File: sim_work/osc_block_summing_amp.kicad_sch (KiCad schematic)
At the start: 4 parts, among them U1 LM4562

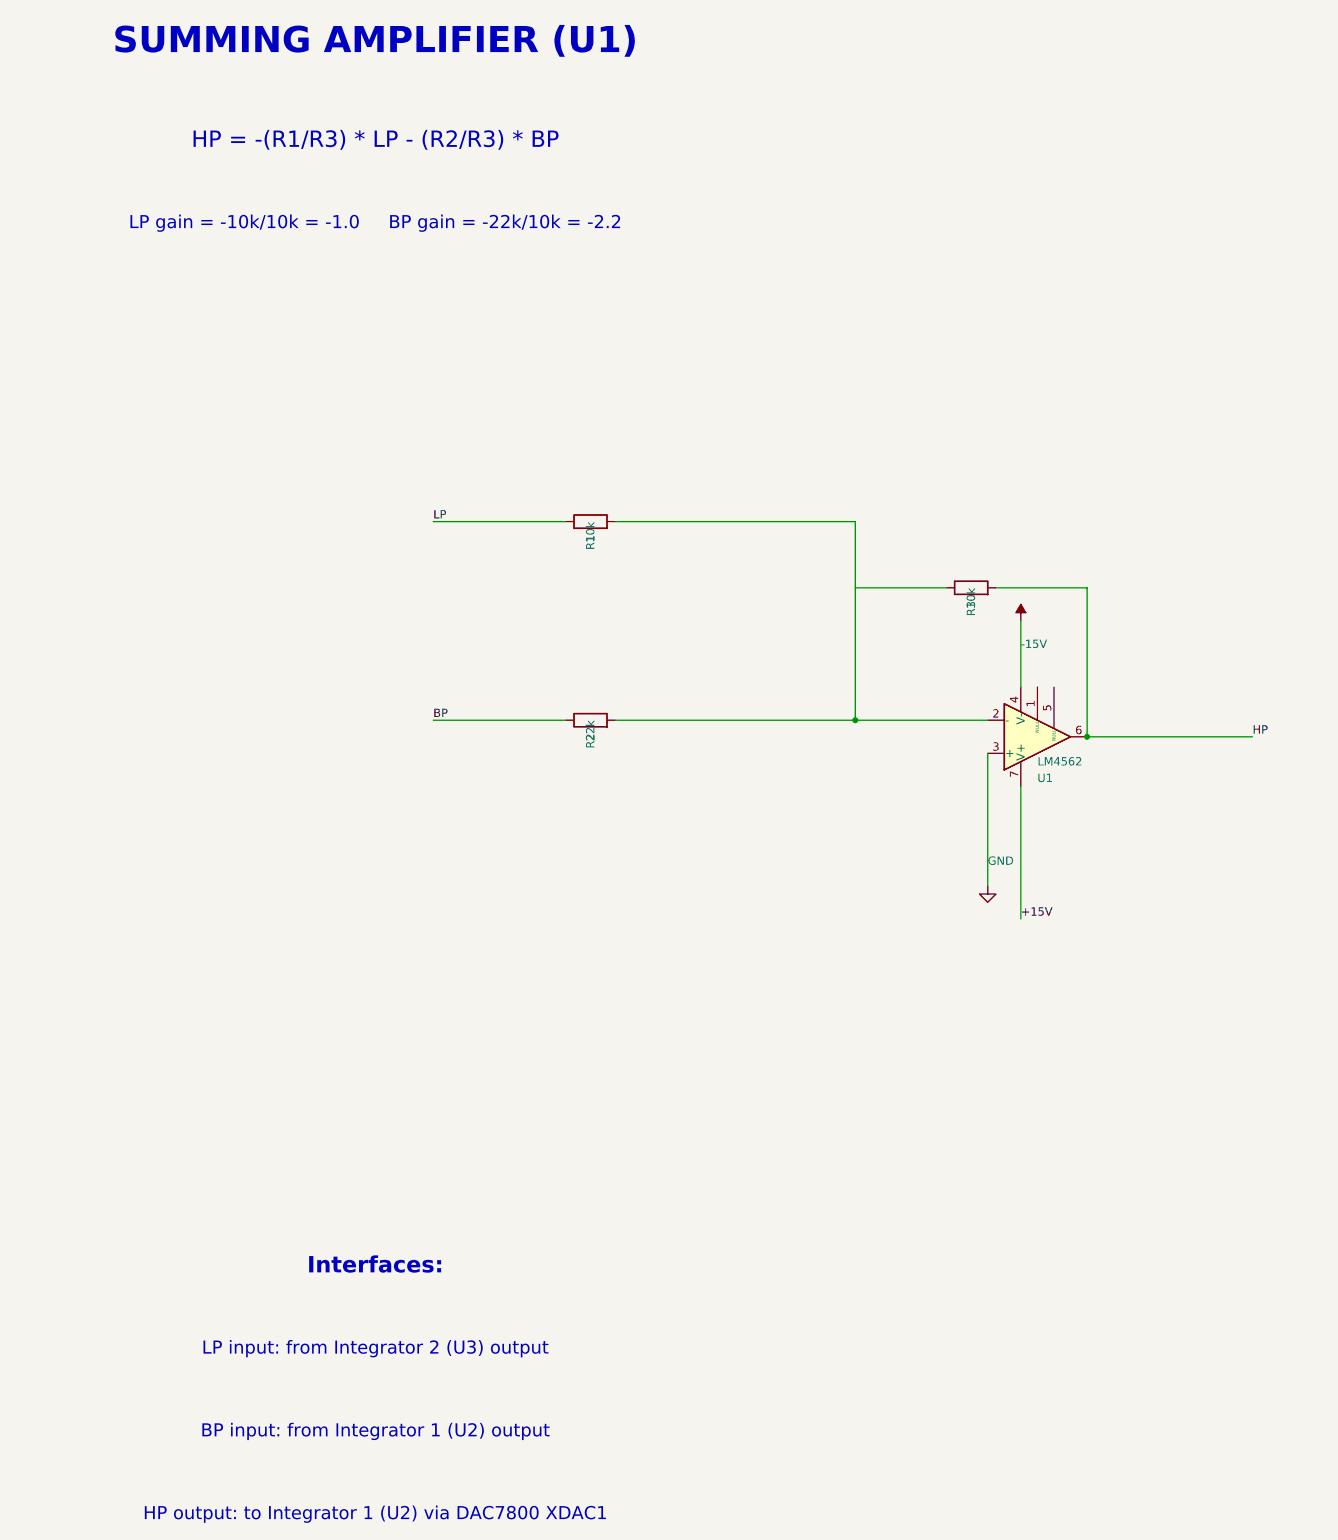
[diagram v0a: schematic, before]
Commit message: Fix schematic connections, add docs and repo portability
- Input filters: R rotation=90 (horizontal), ESD diode rotations fixed,
  junction dots at cathode-signal connection, wires to GND symbols
- Relay ladder: flyback diode rotation 270->90 (K top, A bottom)
- Electrometer/Mux TIA: 4 junction dots each at T-junctions
- AD636 RMS detector: proper IC box with pin labels replaces text-only
- Oscillator blocks: D_Zener symbol, L-shaped cathode routing
- TIA blocks: title/function annotations on all 5 blocks
- New: requirements.txt, docs/oscillator_guide.md
- D_Zener.kicad_sym added to bundled symbols/
- .gitignore updated for docs/ and requirements.txt
- README updated with pip install -r requirements.txt
- PROJECT.md session 9 changelog
- SimGUI builds clean (0 errors)

Co-Authored-By: Claude Opus 4.6 <noreply@anthropic.com>
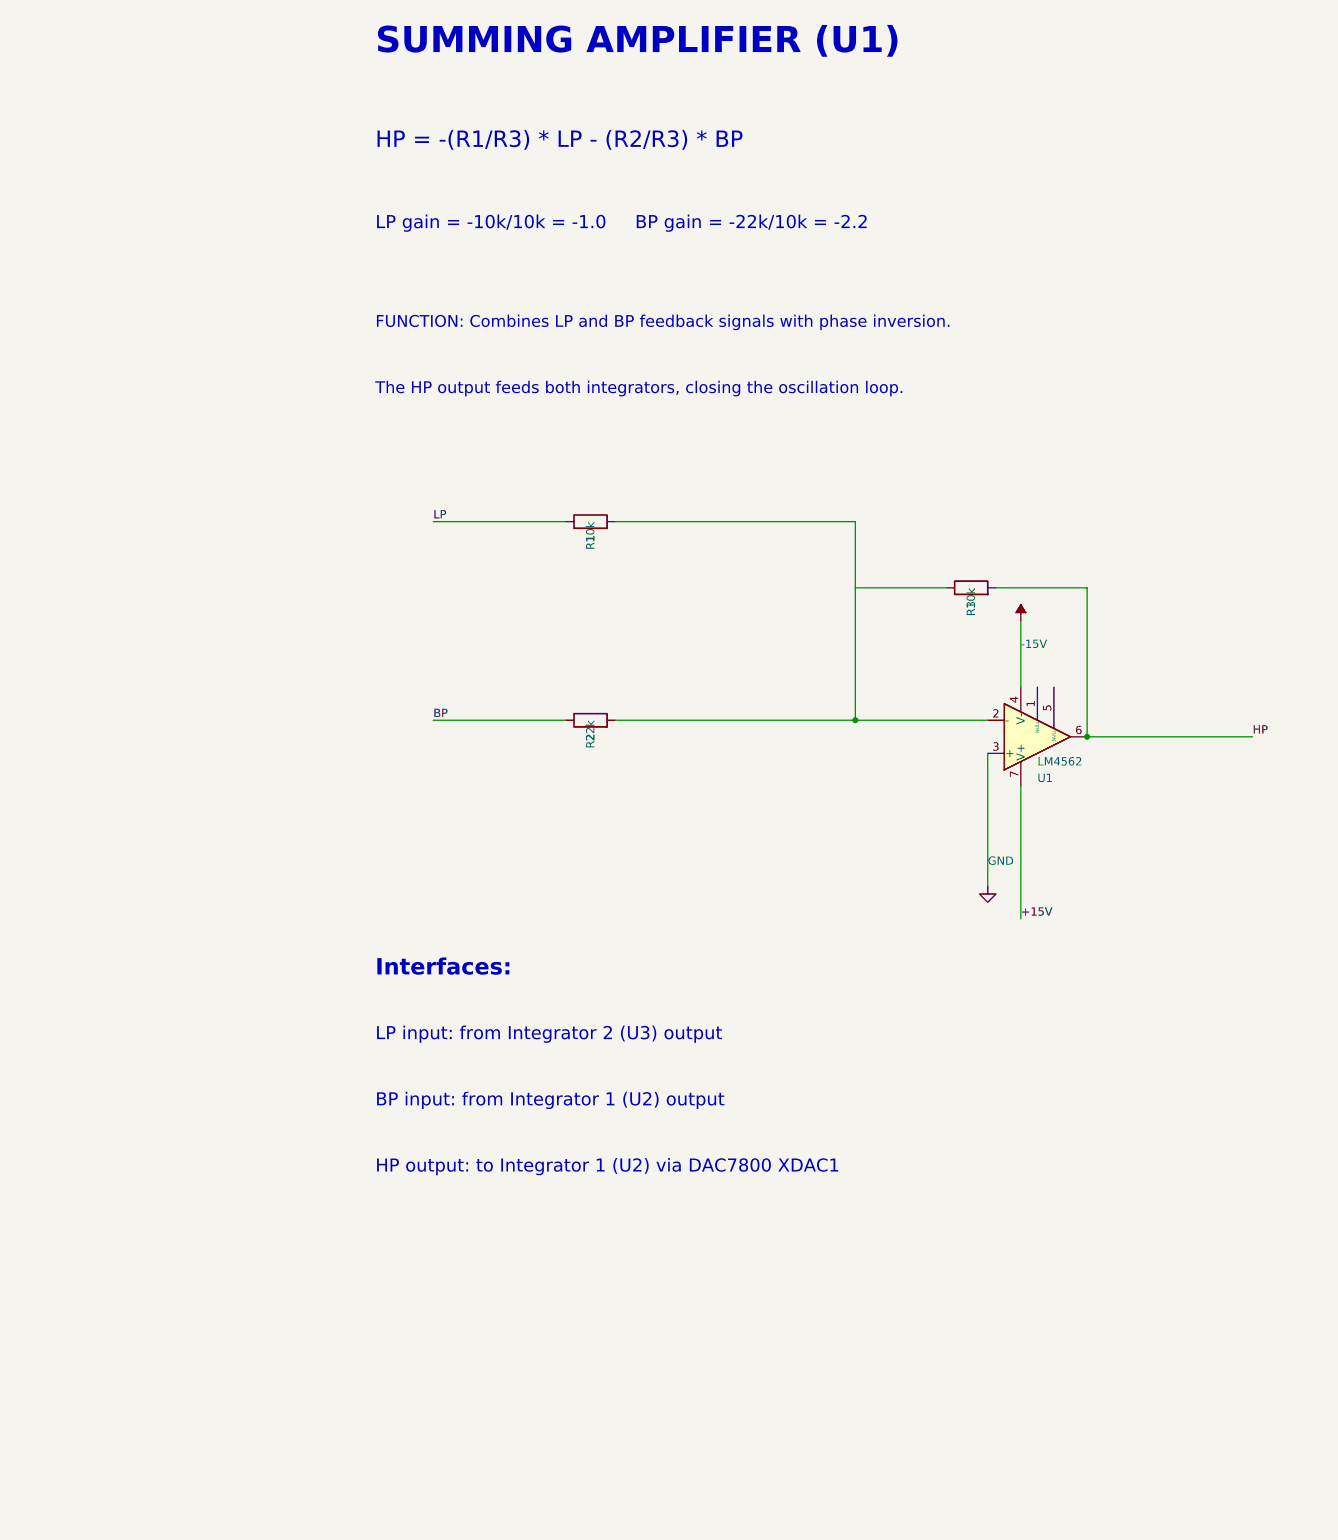
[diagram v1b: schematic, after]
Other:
- note added: "FUNCTION: Combines LP and BP feedback signals with phase inversion."
- note added: "The HP output feeds both integrators, closing the oscillation loop."
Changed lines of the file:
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@@
 		(instances
 			(project "Oscillator - Summing Amplifier"
-				(path "/2c799509-0e7d-405b-bbcf-876a6c7cc8ef"
+				(path "/fb9dc419-e6c7-4f84-8a32-7dc9712e332e"
 					(reference "U1")
 					(unit 1)
@@
 		(instances
 			(project "Oscillator - Summing Amplifier"
-				(path "/2c799509-0e7d-405b-bbcf-876a6c7cc8ef"
+				(path "/fb9dc419-e6c7-4f84-8a32-7dc9712e332e"
 					(reference "R1")
 					(unit 1)
@@
 		(instances
 			(project "Oscillator - Summing Amplifier"
-				(path "/2c799509-0e7d-405b-bbcf-876a6c7cc8ef"
+				(path "/fb9dc419-e6c7-4f84-8a32-7dc9712e332e"
 					(reference "R2")
 					(unit 1)
@@
 		(instances
 			(project "Oscillator - Summing Amplifier"
-				(path "/2c799509-0e7d-405b-bbcf-876a6c7cc8ef"
+				(path "/fb9dc419-e6c7-4f84-8a32-7dc9712e332e"
 					(reference "R3")
 					(unit 1)
@@
 		(instances
 			(project "Oscillator - Summing Amplifier"
-				(path "/2c799509-0e7d-405b-bbcf-876a6c7cc8ef"
+				(path "/fb9dc419-e6c7-4f84-8a32-7dc9712e332e"
 					(reference "#PWR001")
 					(unit 1)
@@
 		(instances
 			(project "Oscillator - Summing Amplifier"
-				(path "/2c799509-0e7d-405b-bbcf-876a6c7cc8ef"
+				(path "/fb9dc419-e6c7-4f84-8a32-7dc9712e332e"
 					(reference "#PWR002")
 					(unit 1)
@@
 				(bold yes)
 			)
+			(justify left)
 		)
 	)
@@
 				(size 2.5 2.5)
 			)
+			(justify left)
 		)
 	)
@@
 				(size 2 2)
 			)
+			(justify left)
+		)
+	)
+	(text "FUNCTION: Combines LP and BP feedback signals with phase inversion."
+		(exclude_from_sim no)
+		(at 20.32 58.42 0.0000)
+		(effects
+			(font
+				(size 1.8 1.8)
+			)
+			(justify left)
+		)
+	)
+	(text "The HP output feeds both integrators, closing the oscillation loop."
+		(exclude_from_sim no)
+		(at 20.32 68.58 0.0000)
+		(effects
+			(font
+				(size 1.8 1.8)
+			)
+			(justify left)
 		)
 	)
 	(text "Interfaces:"
 		(exclude_from_sim no)
-		(at 20.32 203.2 0.0000)
+		(at 20.32 157.48 0.0000)
 		(effects
 			(font
@@
 				(bold yes)
 			)
+			(justify left)
 		)
 	)
 	(text "LP input: from Integrator 2 (U3) output"
 		(exclude_from_sim no)
-		(at 20.32 215.9 0.0000)
+		(at 20.32 167.64 0.0000)
 		(effects
 			(font
 				(size 2 2)
 			)
+			(justify left)
 		)
 	)
 	(text "BP input: from Integrator 1 (U2) output"
 		(exclude_from_sim no)
-		(at 20.32 228.6 0.0000)
+		(at 20.32 177.8 0.0000)
 		(effects
 			(font
 				(size 2 2)
 			)
+			(justify left)
 		)
 	)
 	(text "HP output: to Integrator 1 (U2) via DAC7800 XDAC1"
 		(exclude_from_sim no)
-		(at 20.32 241.3 0.0000)
+		(at 20.32 187.96 0.0000)
 		(effects
 			(font
 				(size 2 2)
 			)
-		)
-	)
+			(justify left)
+		)
+	)

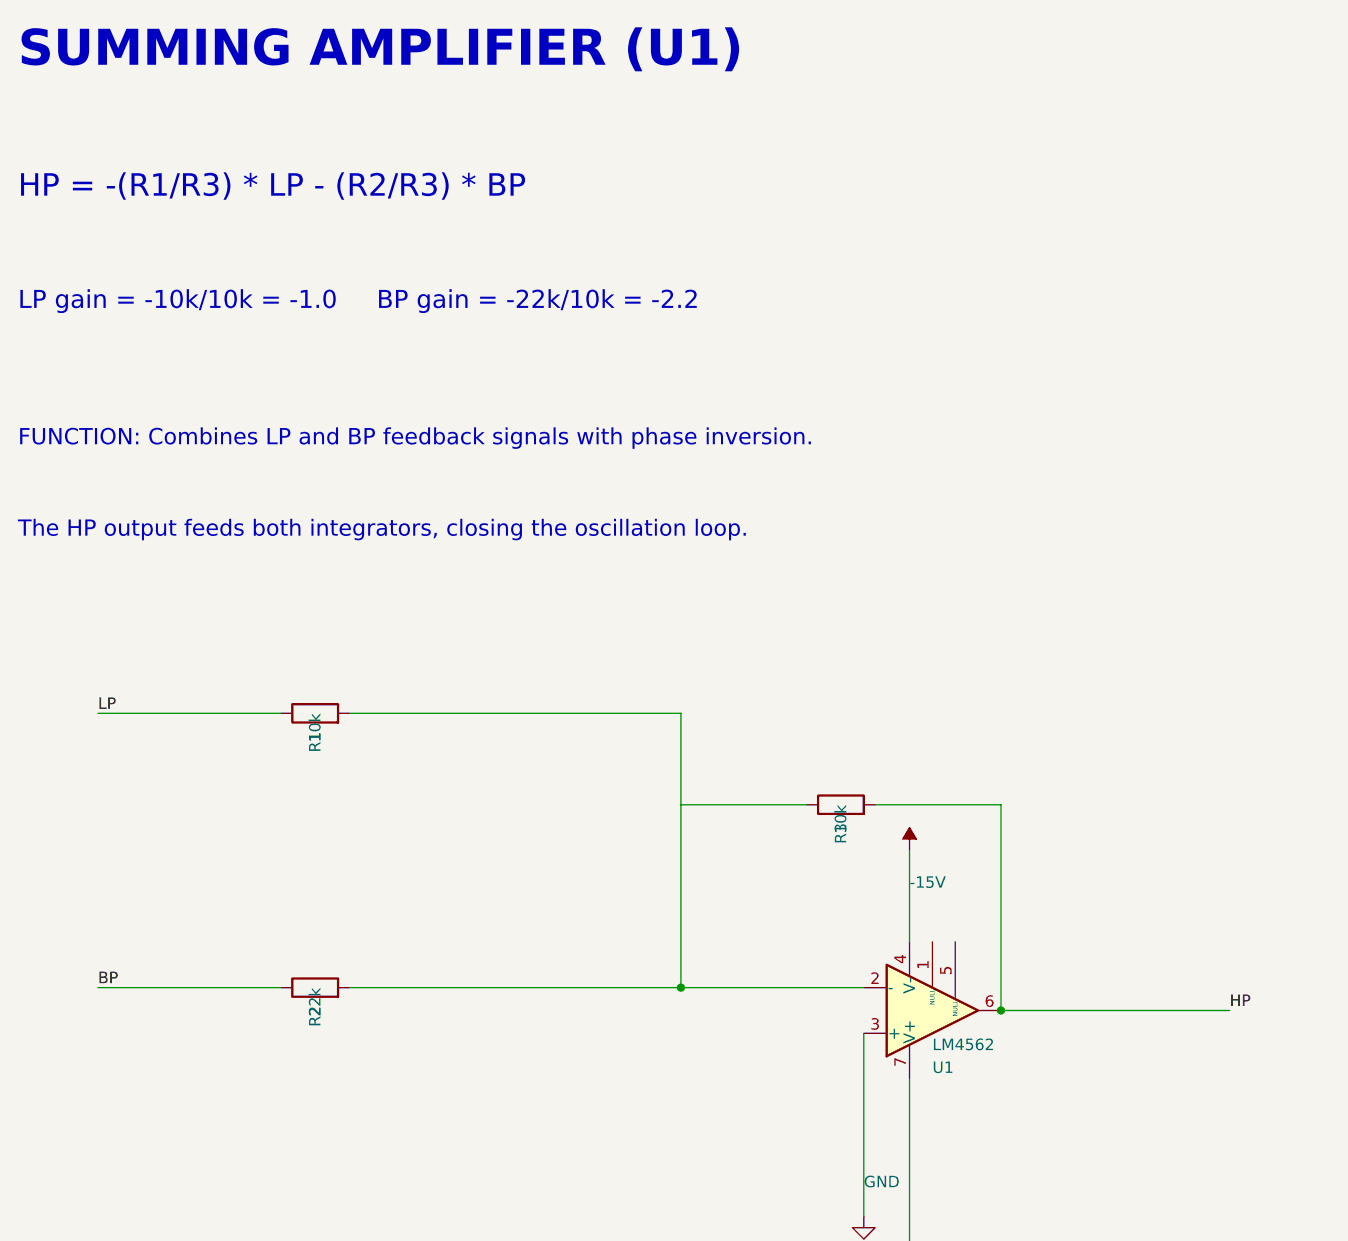
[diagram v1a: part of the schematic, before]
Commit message: Add comparison mode, fix SimGUI subprocess popups, DAC7800 IC boxes
- SimGUI: fix Python path detection (FindPython searches Python312/313/311)
- SimGUI: suppress console popup windows (CREATE_NO_WINDOW for subprocess)
- SimGUI: add Comparison project (MDAC vs Analog oscillator side-by-side)
- SimGUI: fix async wrapping (direct await instead of Task.Run)
- Pipeline: draw DAC7800 as proper IC box with pin labels (VREF/IOUT/VCTRL)
- Pipeline: fix electrometer_362 layout (spacing, junction dots at T-junctions)
- Pipeline: fix summing amp gain annotations (BP=-0.455, not -2.2)
- Pipeline: add analog_osc command for friend's SVF oscillator simulation
- Docs: comparison_guide.md, updated README and PROJECT tracker

Co-Authored-By: Claude Opus 4.6 <noreply@anthropic.com>
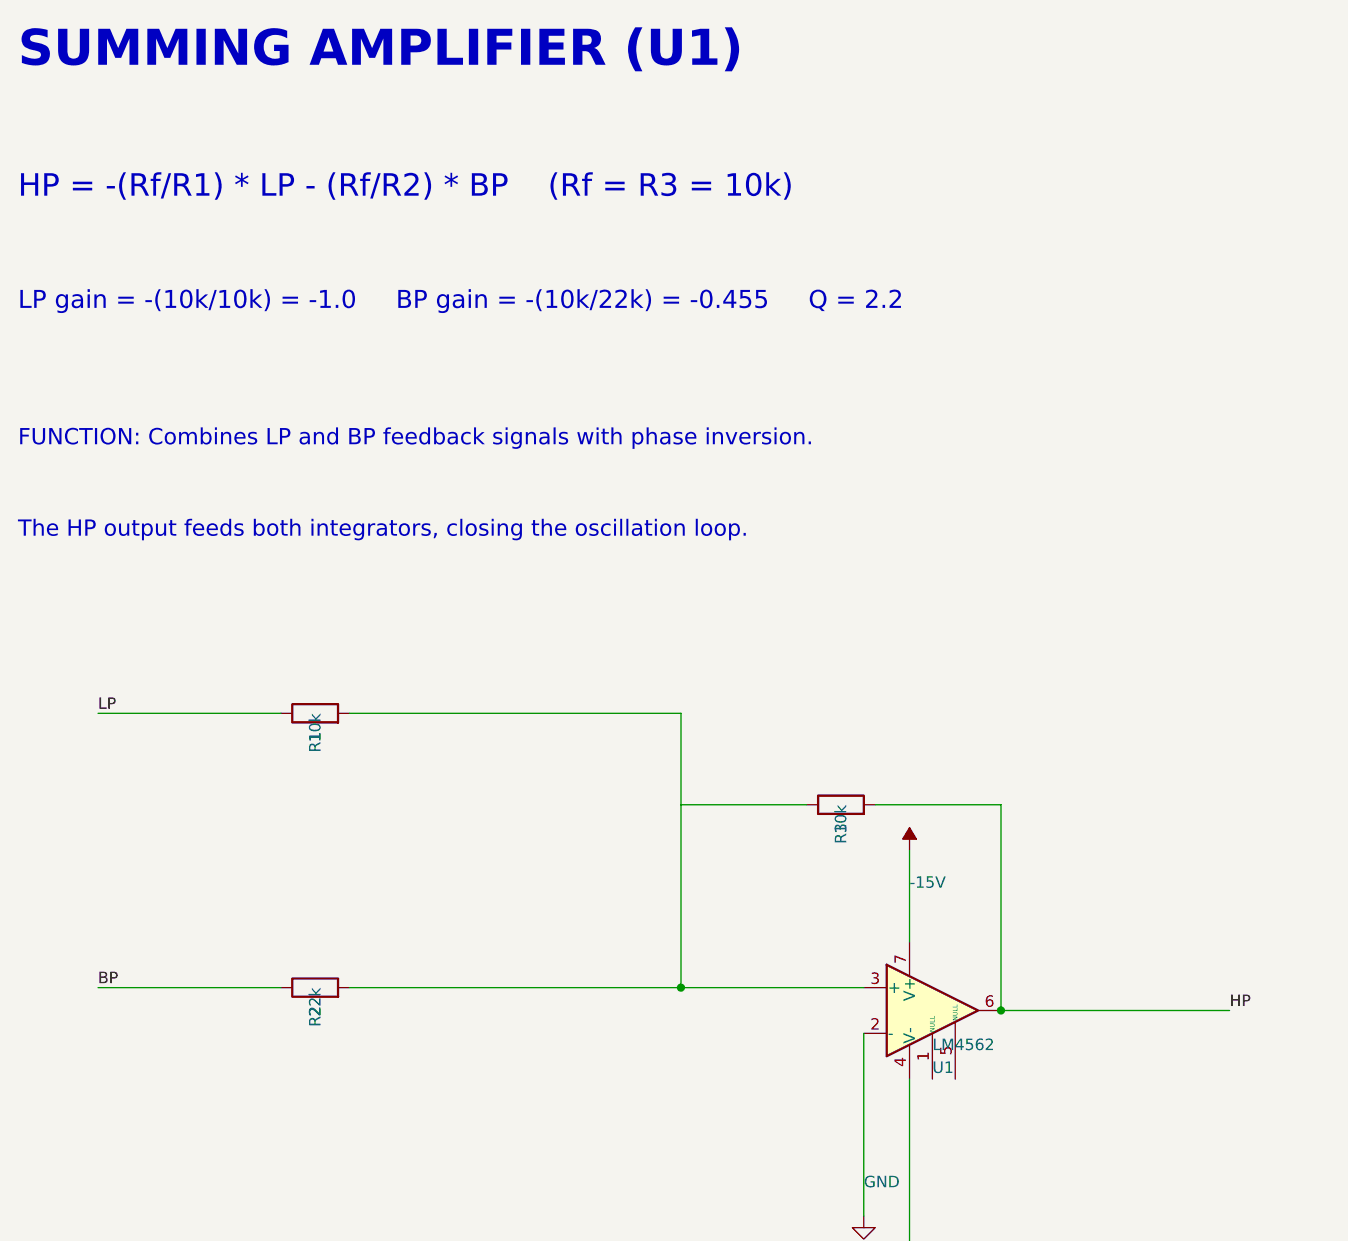
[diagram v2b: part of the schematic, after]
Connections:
- net +15V: now also U1.4 (V-); no longer U1.7 (V+)
- net -15V: now also U1.7 (V+); no longer U1.4 (V-)
- net GND: now also U1.2 (-); no longer U1.3 (+)
- net at R1.2, R2.2: now also U1.3 (+); no longer U1.2 (-)
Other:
- note added: "HP = -(Rf/R1) * LP - (Rf/R2) * BP (Rf = R3 = 10k)"
- note added: "LP gain = -(10k/10k) = -1.0 BP gain = -(10k/22k) = -0.455 Q = 2.2"
- note removed: "HP = -(R1/R3) * LP - (R2/R3) * BP"
- note removed: "LP gain = -10k/10k = -1.0 BP gain = -22k/10k = -2.2"
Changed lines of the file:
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@@
 		(rev "1.0")
 		(company "CircuitForge")
-		(comment 1 "HP = -(R1/R3)*LP - (R2/R3)*BP")
-		(comment 2 "LP gain = -1.0, BP gain = -2.2")
+		(comment 1 "HP = -(Rf/R1)*LP - (Rf/R2)*BP, Rf=R3=10k")
+		(comment 2 "LP gain = -1.0, BP gain = -0.455, Q = 2.2")
 		(comment 3 "Block 1 of 6")
 	)
@@
 		(lib_id "LM741:LM741")
 		(at 121.92 121.92 0)
-		(mirror x)
 		(unit 1)
 		(exclude_from_sim no)
@@
 		(instances
 			(project "Oscillator - Summing Amplifier"
-				(path "/fb9dc419-e6c7-4f84-8a32-7dc9712e332e"
+				(path "/4e5c4214-cbec-4b26-9c46-b0ba11d95c9a"
 					(reference "U1")
 					(unit 1)
@@
 		(instances
 			(project "Oscillator - Summing Amplifier"
-				(path "/fb9dc419-e6c7-4f84-8a32-7dc9712e332e"
+				(path "/4e5c4214-cbec-4b26-9c46-b0ba11d95c9a"
 					(reference "R1")
 					(unit 1)
@@
 		(instances
 			(project "Oscillator - Summing Amplifier"
-				(path "/fb9dc419-e6c7-4f84-8a32-7dc9712e332e"
+				(path "/4e5c4214-cbec-4b26-9c46-b0ba11d95c9a"
 					(reference "R2")
 					(unit 1)
@@
 		(instances
 			(project "Oscillator - Summing Amplifier"
-				(path "/fb9dc419-e6c7-4f84-8a32-7dc9712e332e"
+				(path "/4e5c4214-cbec-4b26-9c46-b0ba11d95c9a"
 					(reference "R3")
 					(unit 1)
@@
 		(instances
 			(project "Oscillator - Summing Amplifier"
-				(path "/fb9dc419-e6c7-4f84-8a32-7dc9712e332e"
+				(path "/4e5c4214-cbec-4b26-9c46-b0ba11d95c9a"
 					(reference "#PWR001")
 					(unit 1)
@@
 		(instances
 			(project "Oscillator - Summing Amplifier"
-				(path "/fb9dc419-e6c7-4f84-8a32-7dc9712e332e"
+				(path "/4e5c4214-cbec-4b26-9c46-b0ba11d95c9a"
 					(reference "#PWR002")
 					(unit 1)
@@
 		)
 	)
-	(text "HP = -(R1/R3) * LP - (R2/R3) * BP"
+	(text "HP = -(Rf/R1) * LP - (Rf/R2) * BP    (Rf = R3 = 10k)"
 		(exclude_from_sim no)
 		(at 20.32 30.48 0.0000)
@@
 		)
 	)
-	(text "LP gain = -10k/10k = -1.0     BP gain = -22k/10k = -2.2"
+	(text "LP gain = -(10k/10k) = -1.0     BP gain = -(10k/22k) = -0.455     Q = 2.2"
 		(exclude_from_sim no)
 		(at 20.32 43.18 0.0000)
